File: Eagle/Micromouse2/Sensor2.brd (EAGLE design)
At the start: 47.9 x 24.1 mm, 21 parts

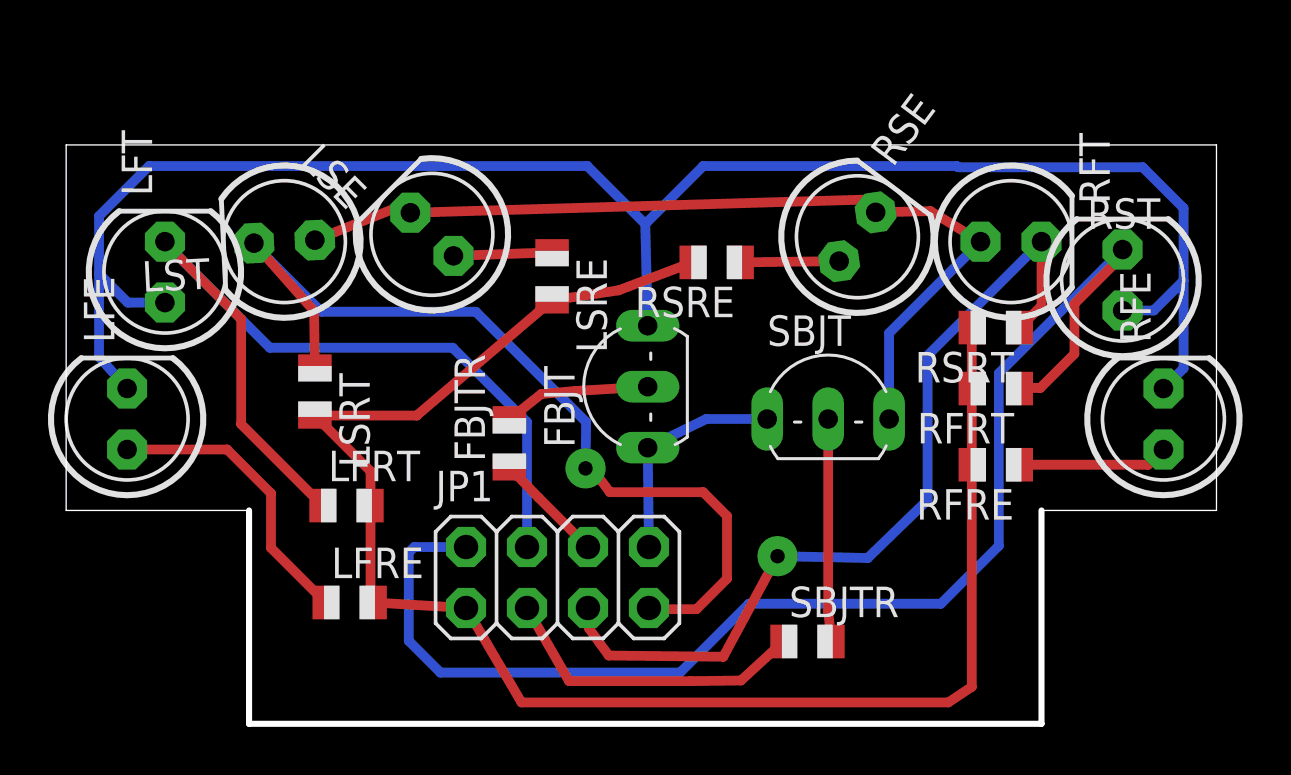
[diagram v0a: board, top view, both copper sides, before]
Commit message: updated eagle files for the sensor
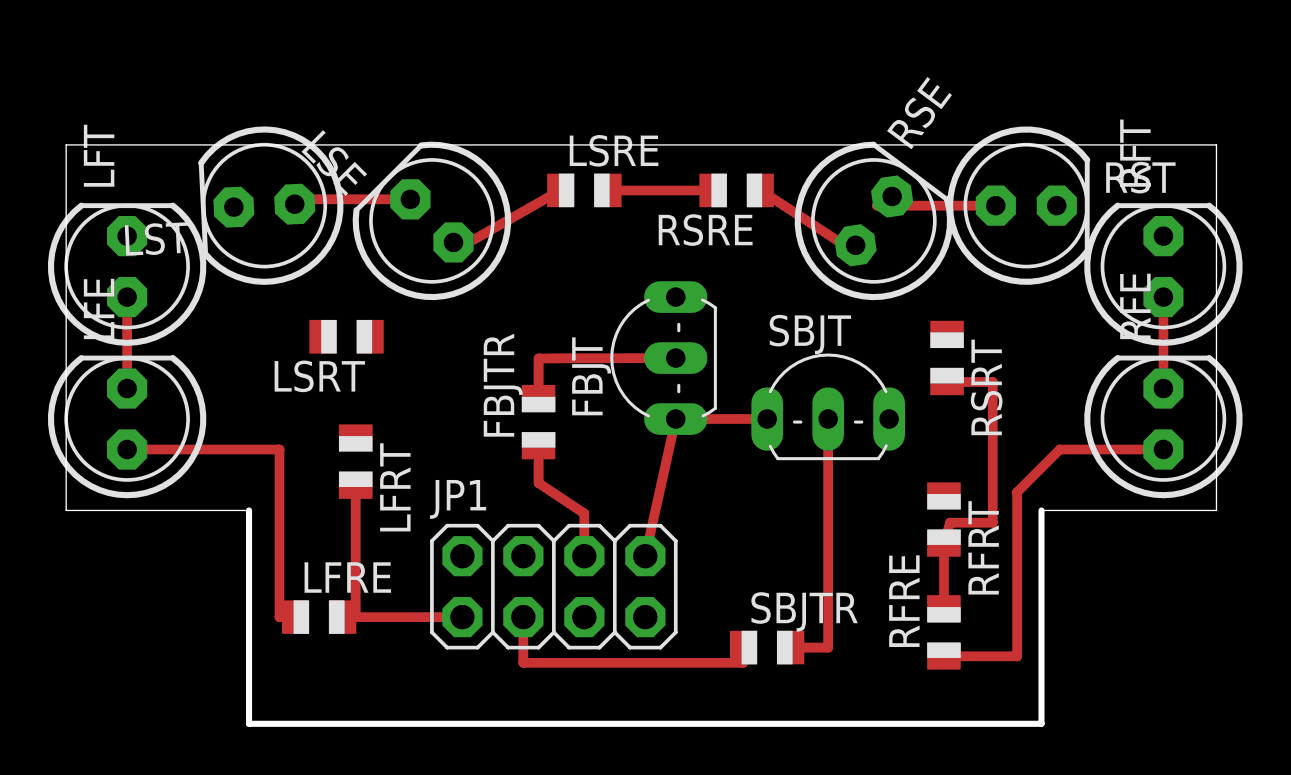
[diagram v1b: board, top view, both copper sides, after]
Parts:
- moved RFRE 7.31 mm to (36.6, -5.08), turned to 90 degrees
- moved RFRT 5.87 mm to (36.6, -0.38), turned to 270 degrees
- moved LSRE 3.83 mm to (21.6, 13.3), turned to 0 degrees
- moved RSRE 3.11 mm to (27.9, 13.3)
- moved LSRT 2.64 mm to (11.7, 7.24), turned to 180 degrees
- moved RSRT 2.40 mm to (36.7, 6.35), turned to 270 degrees
- moved LFRT 1.87 mm to (12.1, 2.03), turned to 270 degrees
- moved RFT 1.79 mm to (45.7, 10.2)
- moved LST 1.72 mm to (8.26, 12.7)
- moved SBJTR 1.70 mm to (29.2, -5.71)
- moved FBJT 1.67 mm to (24.1, 6.35)
- moved RST 1.63 mm to (40.0, 12.7)
- moved LFT 1.59 mm to (2.54, 10.2)
- moved FBJTR 1.51 mm to (19.7, 3.68)
- moved LFRE 1.41 mm to (10.5, -4.45)
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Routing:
- net N$3: track 74.8 -> 7.62 mm
- net FRS: track 56.2 -> 0.00 mm
- net VCC: track 68.9 -> 28.5 mm
- net LS: track 37.6 -> 0.00 mm, vias 1 -> 0
- net FLS: track 37.2 -> 0.00 mm
- net RS: track 35.8 -> 0.00 mm, vias 1 -> 0
- net N$6: track 38.0 -> 10.5 mm
- net N$7: track 6.25 -> 16.7 mm
- net N$5: track 9.28 -> 11.1 mm
- net N$1: track 12.2 -> 14.0 mm
- net SIDE_EN: track 13.1 -> 11.7 mm
- net N$2: track 6.15 -> 7.37 mm
- net FRONT_EN: track 4.66 -> 5.61 mm
- net N$10: track 4.11 -> 5.03 mm
- net N$11: track 4.11 -> 4.61 mm
